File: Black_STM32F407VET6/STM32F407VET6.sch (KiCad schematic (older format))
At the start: 94 parts, among them J1 T0, J10 - HotBed +, J11 Heater0, J12 X-, J13 Y-, J14 Z-, J15 Z+, J16 USB_B, J17 Left Analog, J18 Left Spi, J2 T1, J23 EXP2, J24 LCD2004, J25 Bottom, J26 Right, J28 LIGHTS, J29 Z, J3 TB, J30 Z, J38 X, J39 Y, J4 TC, J41 E0, J43 Heater1, J44 COM, J47 I2C, J48 SPI, J49 SPI, J5 + VIN -, J50 SDIO, J51 Servo, J52 Servo, J53 PowerSelect, J54 Power, J55 PD11, J56 Power, J6 Fan3, J7 Fan2, J8 Fan1, J9 Fan0, Q1 BCX70, Q10 BCX70, Q11 BCX70, Q12 IRLR8726PBF, Q13 IRLR8726PBF, Q14 IRLR8726PBF, Q2 BCX70, Q3 BCX70, Q4 IRLML0030TRPBF, Q5 BCX70, Q6 IRLML0030TRPBF, Q7 IRLML0030TRPBF, Q8 IRLML0030TRPBF, Q9 BCX70, SW1 Boot0, U5 AT24CS01-SSHM

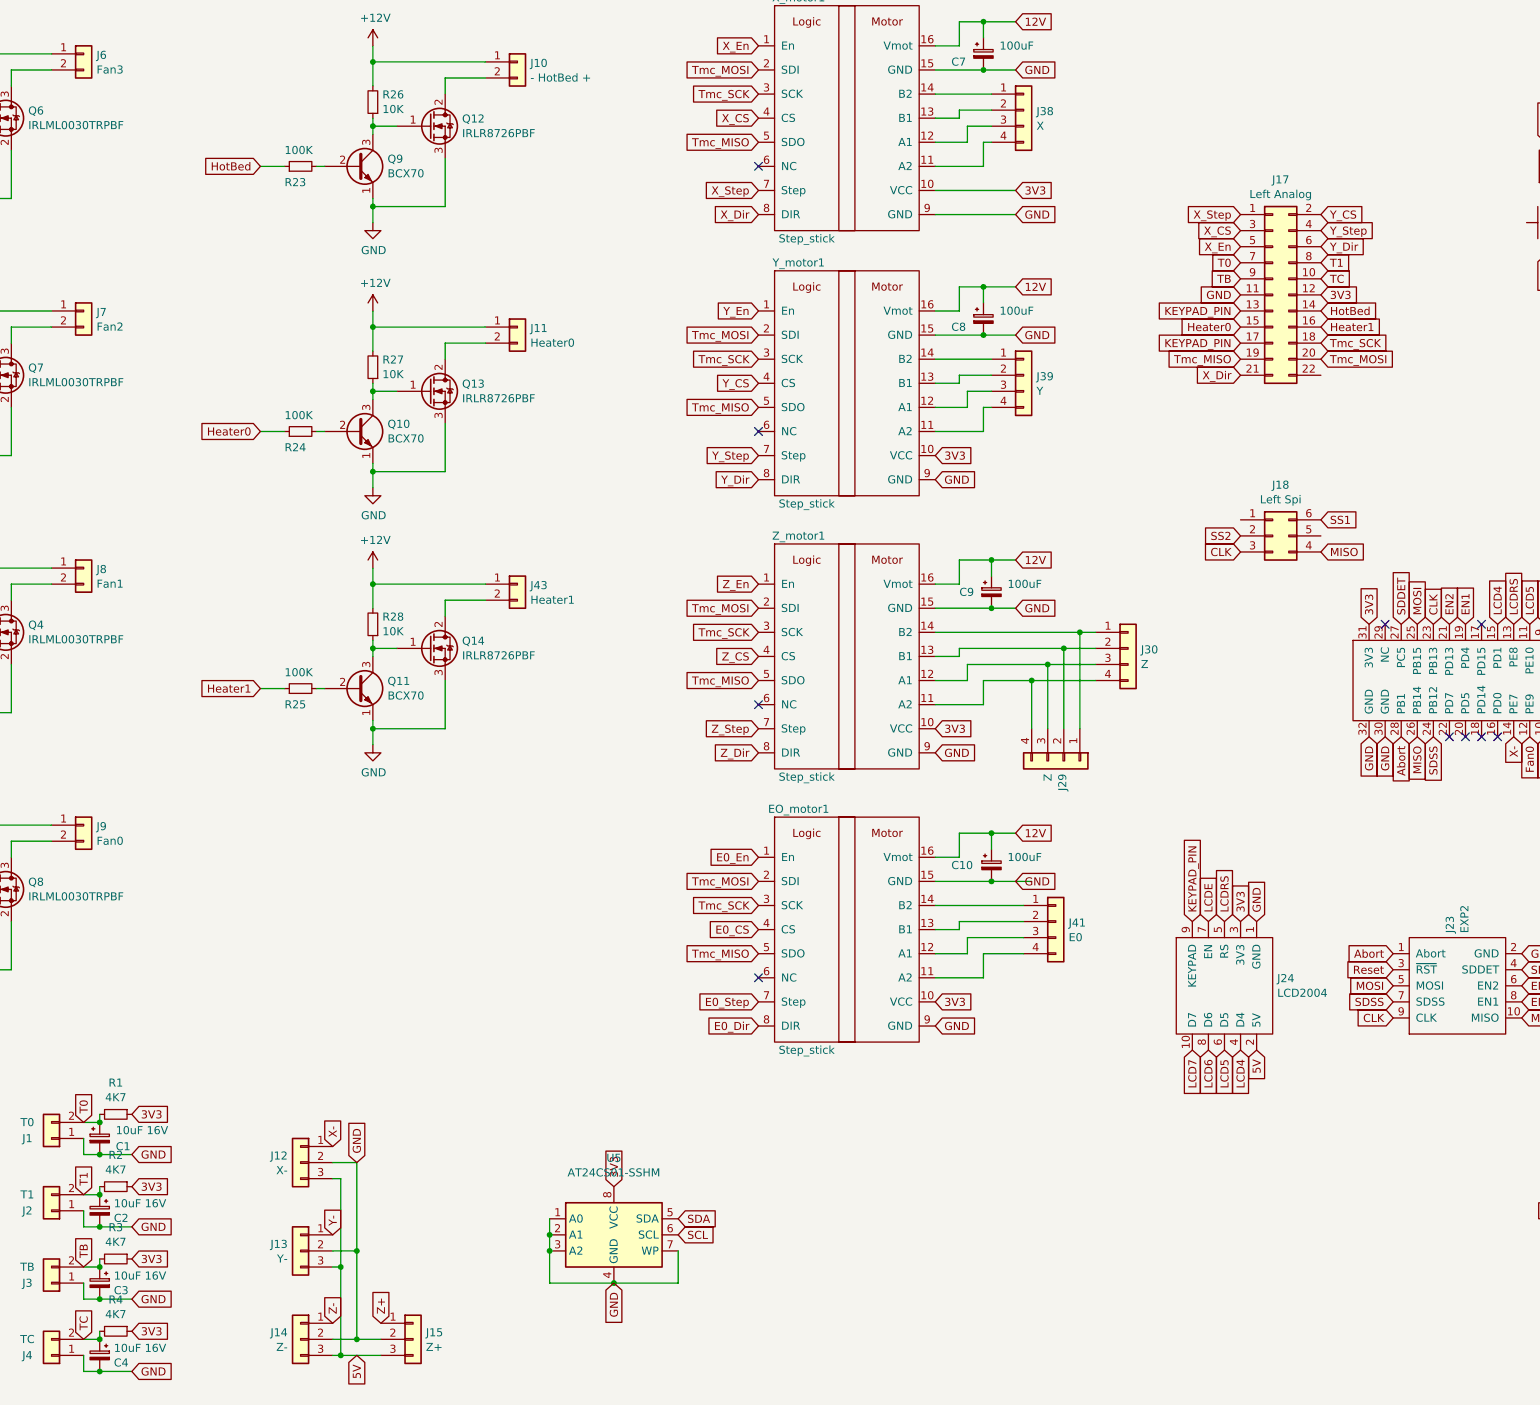
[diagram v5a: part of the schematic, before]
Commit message: Left side  - Temperature sensors  - Capacitor package change  - Reworked left side symbols
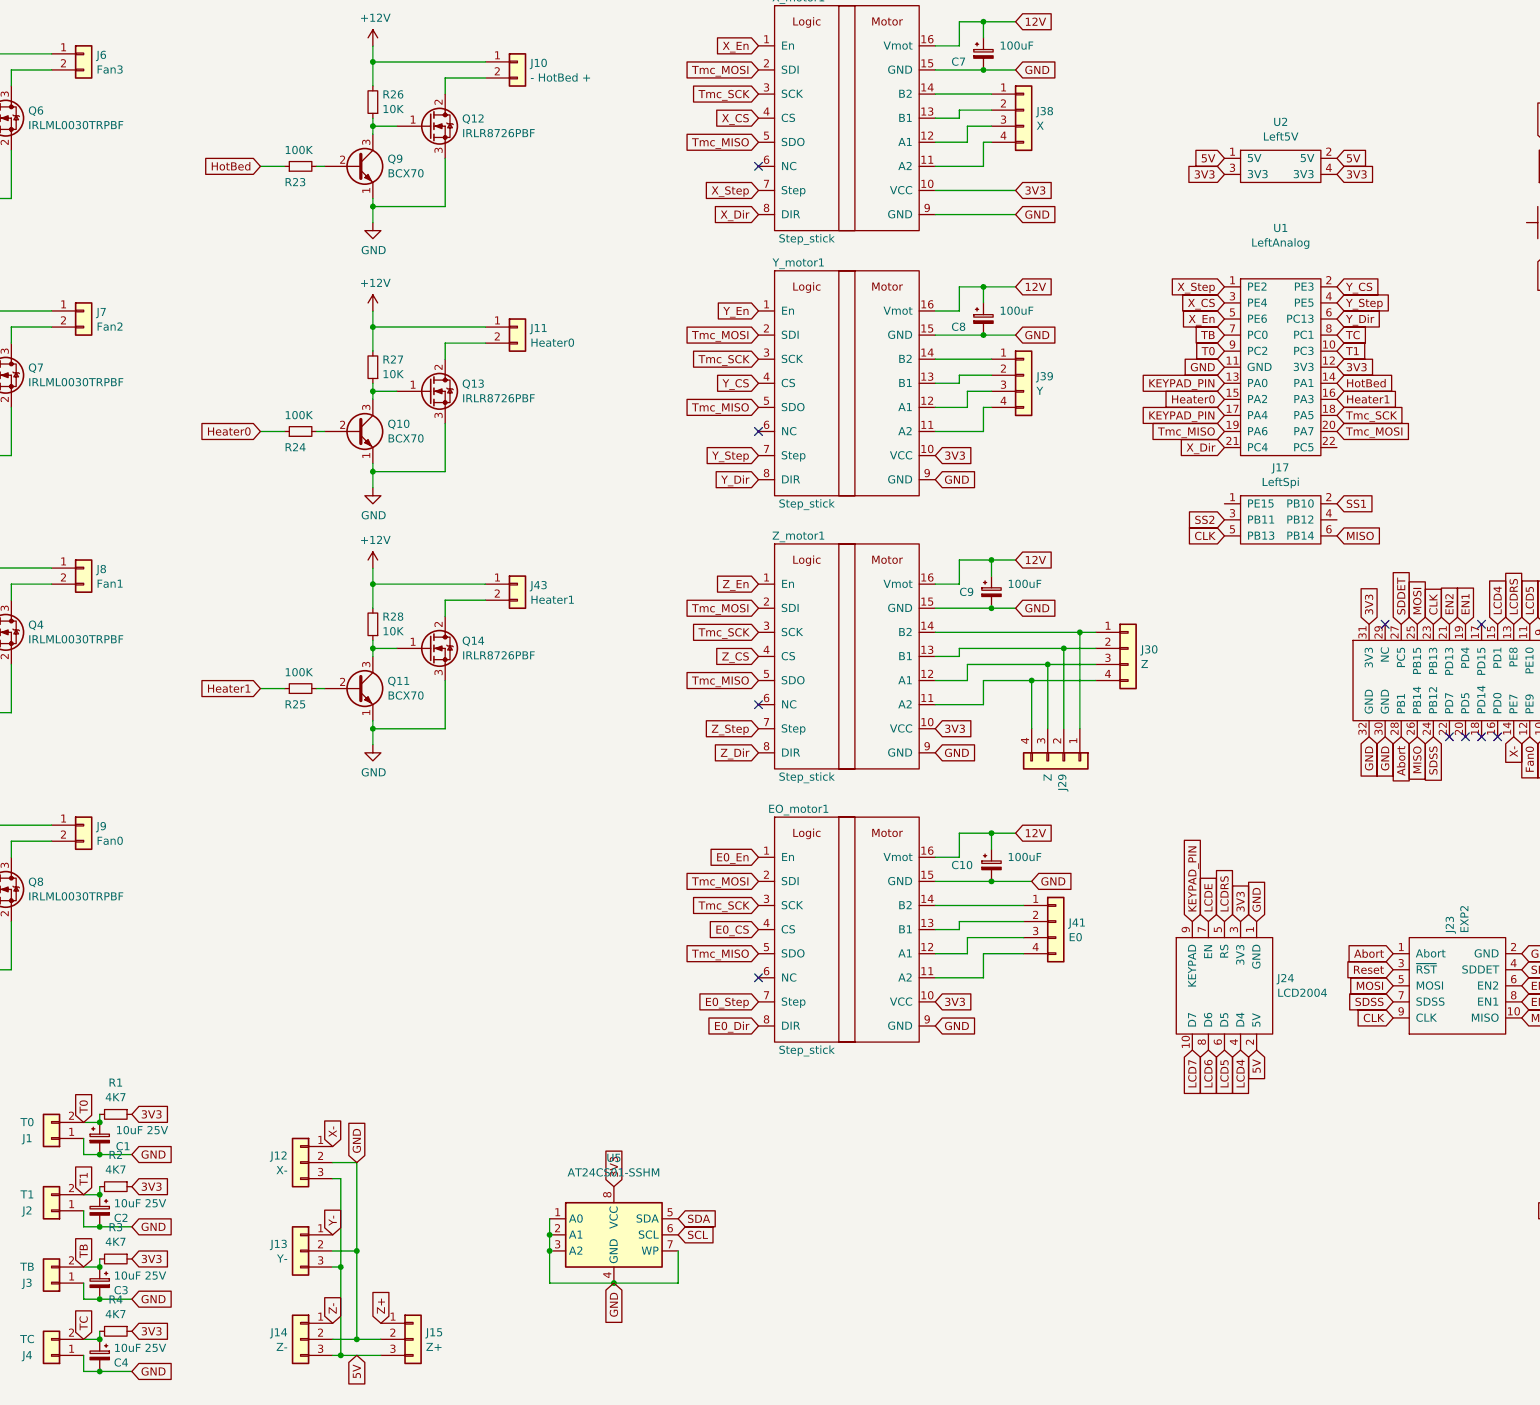
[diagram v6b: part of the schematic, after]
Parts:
- removed J17: Left Analog, Connector_PinHeader_2.54mm:PinHeader_2x11_P2.54mm_Vertical, symbol Connector_Generic:Conn_02x11_Odd_Even
- removed J18: Left Spi, Connector_PinHeader_2.54mm:PinHeader_2x03_P2.54mm_Vertical, symbol Connector_Generic:Conn_02x03_Counter_Clockwise
- added J17: LeftSpi, Connector_PinHeader_2.54mm:PinHeader_2x03_P2.54mm_Vertical, symbol STM32F407VET6:LeftSpi
- added U1: LeftAnalog, Connector_PinHeader_2.54mm:PinHeader_2x11_P2.54mm_Vertical, symbol STM32F407VET6:LeftAnalog
- added U2: Left5V, Connector_PinHeader_2.54mm:PinHeader_2x02_P2.54mm_Vertical, symbol STM32F407VET6:Left5V
- C1, C2, C3, C4: value 10uF 16V -> 10uF 25V; footprint Capacitor_THT:CP_Radial_D5.0mm_P2.00mm -> Capacitor_THT:CP_Radial_D4.0mm_P2.00mm
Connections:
- net +3V3: now also U1.12 (3V3), U2.3 (3V3), U2.4 (3V3)
- net +5V: now also U2.1 (5V), U2.2 (5V)
- net CLK: now also J17.5 (PB13)
- net GND: now also U1.11 (GND)
- net Heater0: now also U1.15 (PA2)
- net Heater1: now also U1.16 (PA3)
- net HotBed: now also U1.14 (PA1)
- net KEYPAD_PIN: now also U1.13 (PA0), U1.17 (PA4)
- net MISO: now also J17.6 (PB14)
- net SS1: now also J17.2 (PB10)
- net SS2: now also J17.3 (PB11)
- net T0: now also U1.9 (PC2)
- net T1: now also U1.10 (PC3)
- net TB: now also U1.7 (PC0)
- net TC: now also U1.8 (PC1)
- net Tmc_MISO: now also U1.19 (PA6)
- net Tmc_MOSI: now also U1.20 (PA7)
- net Tmc_SCK: now also U1.18 (PA5)
- net X_CS: now also U1.3 (PE4)
- net X_Dir: now also U1.21 (PC4)
- net X_En: now also U1.5 (PE6)
- net X_Step: now also U1.1 (PE2)
- net Y_CS: now also U1.2 (PE3)
- net Y_Dir: now also U1.6 (PC13)
- net Y_Step: now also U1.4 (PE5)
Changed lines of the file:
@@
 P 2800 8100
 F 0 "C1" H 2900 8050 50  0000 L CNN
-F 1 "10uF 16V" H 2900 8150 50  0000 L CNN
-F 2 "Capacitor_THT:CP_Radial_D5.0mm_P2.00mm" H 2800 8100 50  0001 C CNN
+F 1 "10uF 25V" H 2900 8150 50  0000 L CNN
+F 2 "Capacitor_THT:CP_Radial_D4.0mm_P2.00mm" H 2800 8100 50  0001 C CNN
 F 3 "~" H 2800 8100 50  0001 C CNN
 	1    2800 8100
@@
 P 2800 8550
 F 0 "C2" H 2712 8504 50  0000 R CNN
-F 1 "10uF 16V" H 2712 8595 50  0000 R CNN
-F 2 "Capacitor_THT:CP_Radial_D5.0mm_P2.00mm" H 2800 8550 50  0001 C CNN
+F 1 "10uF 25V" H 2712 8595 50  0000 R CNN
+F 2 "Capacitor_THT:CP_Radial_D4.0mm_P2.00mm" H 2800 8550 50  0001 C CNN
 F 3 "~" H 2800 8550 50  0001 C CNN
 	1    2800 8550
@@
 P 2800 9000
 F 0 "C3" H 2712 8954 50  0000 R CNN
-F 1 "10uF 16V" H 2712 9045 50  0000 R CNN
-F 2 "Capacitor_THT:CP_Radial_D5.0mm_P2.00mm" H 2800 9000 50  0001 C CNN
+F 1 "10uF 25V" H 2712 9045 50  0000 R CNN
+F 2 "Capacitor_THT:CP_Radial_D4.0mm_P2.00mm" H 2800 9000 50  0001 C CNN
 F 3 "~" H 2800 9000 50  0001 C CNN
 	1    2800 9000
@@
 P 2800 9450
 F 0 "C4" H 2712 9404 50  0000 R CNN
-F 1 "10uF 16V" H 2712 9495 50  0000 R CNN
-F 2 "Capacitor_THT:CP_Radial_D5.0mm_P2.00mm" H 2800 9450 50  0001 C CNN
+F 1 "10uF 25V" H 2712 9495 50  0000 R CNN
+F 2 "Capacitor_THT:CP_Radial_D4.0mm_P2.00mm" H 2800 9450 50  0001 C CNN
 F 3 "~" H 2800 9450 50  0001 C CNN
 	1    2800 9450
@@
 Text GLabel 8000 7250 2    50   Input ~ 0
 3V3
-Text GLabel 8500 6500 2    50   Input ~ 0
+Text GLabel 8600 6500 2    50   Input ~ 0
 GND
 Text GLabel 8000 7400 2    50   Input ~ 0
@@
 NoConn ~ 6900 5400
 NoConn ~ 6900 7100
-$Comp
-L Connector_Generic:Conn_02x03_Counter_Clockwise J18
-U 1 1 5D7813B1
-P 10100 4350
-F 0 "J18" H 10150 4667 50  0000 C CNN
-F 1 "Left Spi" H 10150 4576 50  0000 C CNN
-F 2 "Connector_PinHeader_2.54mm:PinHeader_2x03_P2.54mm_Vertical" H 10100 4350 50  0001 C CNN
-F 3 "~" H 10100 4350 50  0001 C CNN
-	1    10100 4350
-	1    0    0    -1
-$EndComp
-$Comp
-L Connector_Generic:Conn_02x11_Odd_Even J17
-U 1 1 5D7A7A3C
-P 10100 2850
-F 0 "J17" H 10150 3567 50  0000 C CNN
-F 1 "Left Analog" H 10150 3476 50  0000 C CNN
-F 2 "Connector_PinHeader_2.54mm:PinHeader_2x11_P2.54mm_Vertical" H 10100 2850 50  0001 C CNN
-F 3 "~" H 10100 2850 50  0001 C CNN
-	1    10100 2850
-	1    0    0    -1
-$EndComp
-Text GLabel 10400 4250 2    50   Input ~ 0
+Text GLabel 10500 4150 2    50   Input ~ 0
 SS1
-Text GLabel 10400 4450 2    50   Input ~ 0
+Text GLabel 10500 4350 2    50   Input ~ 0
 MISO
-Text GLabel 9900 4450 0    50   Input ~ 0
+Text GLabel 9800 4350 0    50   Input ~ 0
 CLK
-Text GLabel 9900 4350 0    50   Input ~ 0
+Text GLabel 9800 4250 0    50   Input ~ 0
 SS2
-Text GLabel 10400 2850 2    50   Input ~ 0
-3V3
-Text GLabel 10400 2650 2    50   Input ~ 0
+Text GLabel 10500 3300 2    50   Input ~ 0
+3V3
+Text GLabel 10500 3200 2    50   Input ~ 0
 T1
-Text GLabel 10400 2750 2    50   Input ~ 0
+Text GLabel 10500 3100 2    50   Input ~ 0
 TC
-Text GLabel 10400 2550 2    50   Input ~ 0
+Text GLabel 10500 3000 2    50   Input ~ 0
 Y_Dir
-Text GLabel 10400 2450 2    50   Input ~ 0
+Text GLabel 10500 2900 2    50   Input ~ 0
 Y_Step
-Text GLabel 10400 2950 2    50   Input ~ 0
+Text GLabel 10500 3400 2    50   Input ~ 0
 HotBed
-Text GLabel 10400 3050 2    50   Input ~ 0
+Text GLabel 10500 3500 2    50   Input ~ 0
 Heater1
-Text GLabel 10400 3150 2    50   Input ~ 0
+Text GLabel 10500 3600 2    50   Input ~ 0
 Tmc_SCK
-Text GLabel 10400 3250 2    50   Input ~ 0
+Text GLabel 10500 3700 2    50   Input ~ 0
 Tmc_MOSI
-Text GLabel 10400 2350 2    50   Input ~ 0
+Text GLabel 10500 2800 2    50   Input ~ 0
 Y_CS
-Text GLabel 9900 2850 0    50   Input ~ 0
-GND
-Text GLabel 9900 2650 0    50   Input ~ 0
+Text GLabel 9800 3300 0    50   Input ~ 0
+GND
+Text GLabel 9800 3200 0    50   Input ~ 0
 T0
-Text GLabel 9900 2750 0    50   Input ~ 0
+Text GLabel 9800 3100 0    50   Input ~ 0
 TB
-Text GLabel 9900 3050 0    50   Input ~ 0
+Text GLabel 9800 3500 0    50   Input ~ 0
 Heater0
-Text GLabel 9900 3350 0    50   Input ~ 0
+Text GLabel 9800 3800 0    50   Input ~ 0
 X_Dir
-Text GLabel 9900 2350 0    50   Input ~ 0
+Text GLabel 9800 2800 0    50   Input ~ 0
 X_Step
-Text GLabel 9900 2550 0    50   Input ~ 0
+Text GLabel 9800 3000 0    50   Input ~ 0
 X_En
-Text GLabel 9900 3250 0    50   Input ~ 0
+Text GLabel 9800 3700 0    50   Input ~ 0
 Tmc_MISO
-Text GLabel 9900 2950 0    50   Input ~ 0
+Text GLabel 9800 3400 0    50   Input ~ 0
 KEYPAD_PIN
-Text GLabel 9900 2450 0    50   Input ~ 0
+Text GLabel 9800 2900 0    50   Input ~ 0
 X_CS
-Text GLabel 9900 3150 0    50   Input ~ 0
+Text GLabel 9800 3600 0    50   Input ~ 0
 KEYPAD_PIN
+$Comp
+L STM32F407VET6:LeftAnalog U1
+U 1 1 5D47DD57
+P 10150 3350
+F 0 "U1" H 10150 4265 50  0000 C CNN
+F 1 "LeftAnalog" H 10150 4174 50  0000 C CNN
+F 2 "Connector_PinHeader_2.54mm:PinHeader_2x11_P2.54mm_Vertical" H 10150 4100 50  0001 C CNN
+F 3 "" H 10150 4100 50  0001 C CNN
+	1    10150 3350
+	1    0    0    -1
+$EndComp
+$Comp
+L STM32F407VET6:LeftSpi J17
+U 1 1 5D4F50E7
+P 10150 4250
+F 0 "J17" H 10150 4575 50  0000 C CNN
+F 1 "LeftSpi" H 10150 4484 50  0000 C CNN
+F 2 "Connector_PinHeader_2.54mm:PinHeader_2x03_P2.54mm_Vertical" H 10150 4500 50  0001 C CNN
+F 3 "" H 10150 4500 50  0001 C CNN
+	1    10150 4250
+	1    0    0    -1
+$EndComp
+Text GLabel 9800 2100 0    50   Input ~ 0
+3V3
+Text GLabel 10500 2100 2    50   Input ~ 0
+3V3
+Text GLabel 9800 2000 0    50   Input ~ 0
+5V
+Text GLabel 10500 2000 2    50   Input ~ 0
+5V
+$Comp
+L STM32F407VET6:Left5V U2
+U 1 1 5D592F71
+P 10150 2150
+F 0 "U2" H 10150 2525 50  0000 C CNN
+F 1 "Left5V" H 10150 2434 50  0000 C CNN
+F 2 "Connector_PinHeader_2.54mm:PinHeader_2x02_P2.54mm_Vertical" H 10150 2500 50  0001 C CNN
+F 3 "" H 10150 2500 50  0001 C CNN
+	1    10150 2150
+	1    0    0    -1
+$EndComp
 $EndSCHEMATC

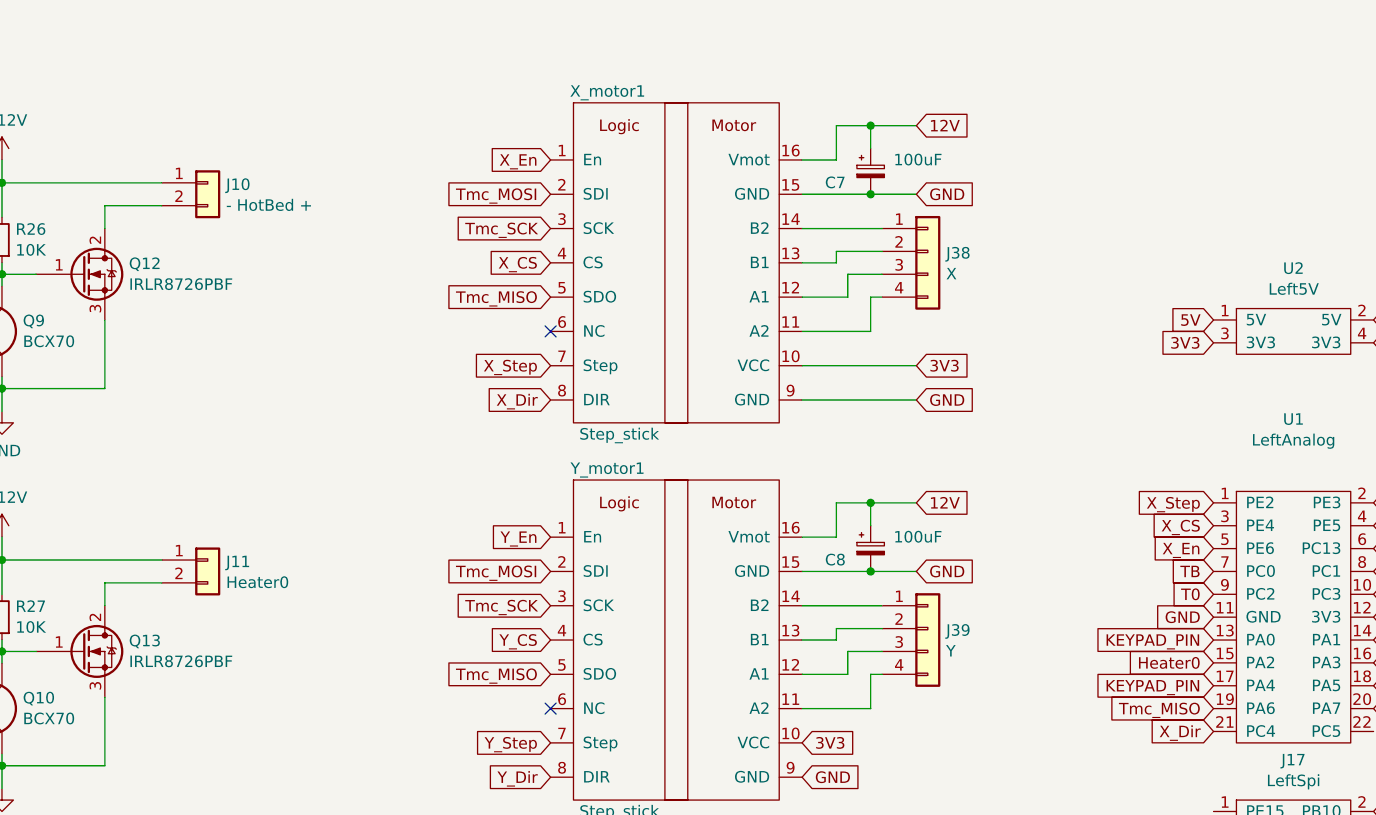
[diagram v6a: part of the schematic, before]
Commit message: Layout finialized  - finished fan section  - fixed & finished temperature section  - drivers positioned roughly
Signed-off-by: Slinta <Slinta000@gmail.com>
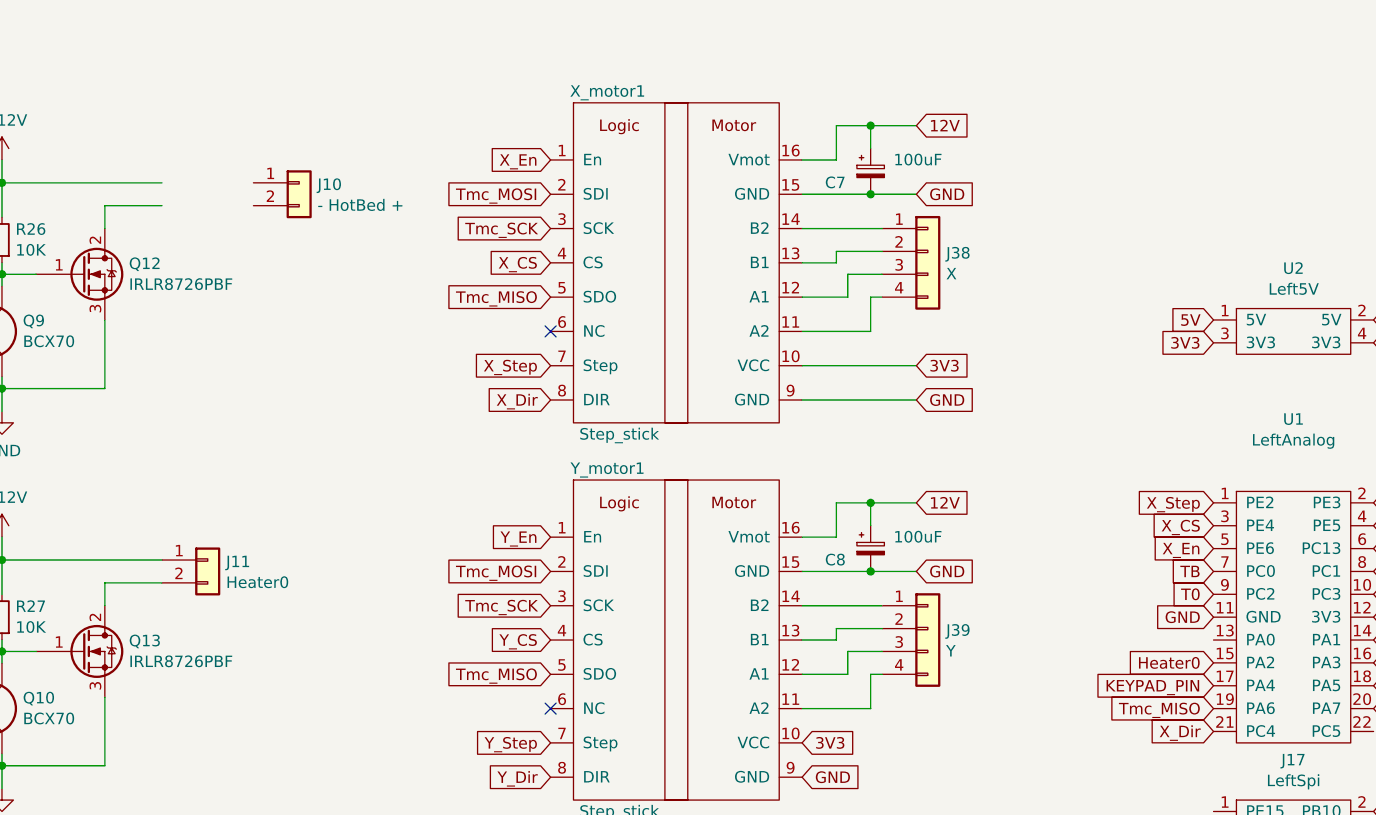
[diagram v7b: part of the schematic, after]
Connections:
- net +12V: no longer J10.1 (Pin_1)
- net KEYPAD_PIN: no longer U1.13 (PA0)
- net at J10.2 (Pin_2): no longer Q12.2 (D)
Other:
- moved on the sheet: J10
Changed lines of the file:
@@
 L Connector_Generic:Conn_01x02 J10
 U 1 1 5D53C77B
-P 5400 1400
-F 0 "J10" H 5480 1392 50  0000 L CNN
-F 1 "- HotBed +" H 5480 1301 50  0000 L CNN
-F 2 "SH_Connectors:KF7.62_2P" H 5400 1400 50  0001 C CNN
-F 3 "~" H 5400 1400 50  0001 C CNN
-	1    5400 1400
+P 5800 1400
+F 0 "J10" H 5880 1392 50  0000 L CNN
+F 1 "- HotBed +" H 5880 1301 50  0000 L CNN
+F 2 "SH_Connectors:KF7.62_2P" H 5800 1400 50  0001 C CNN
+F 3 "~" H 5800 1400 50  0001 C CNN
+	1    5800 1400
 	1    0    0    -1
 $EndComp
@@
 Text GLabel 9800 3700 0    50   Input ~ 0
 Tmc_MISO
-Text GLabel 9800 3400 0    50   Input ~ 0
-KEYPAD_PIN
 Text GLabel 9800 2900 0    50   Input ~ 0
 X_CS
